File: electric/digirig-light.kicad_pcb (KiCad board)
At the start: 2 copper layers, 12.2 x 37.9 mm, 22 parts, among them J1 USB_A, J2 PJ-320A, Q1 MMBT5551L, U1 CM108B

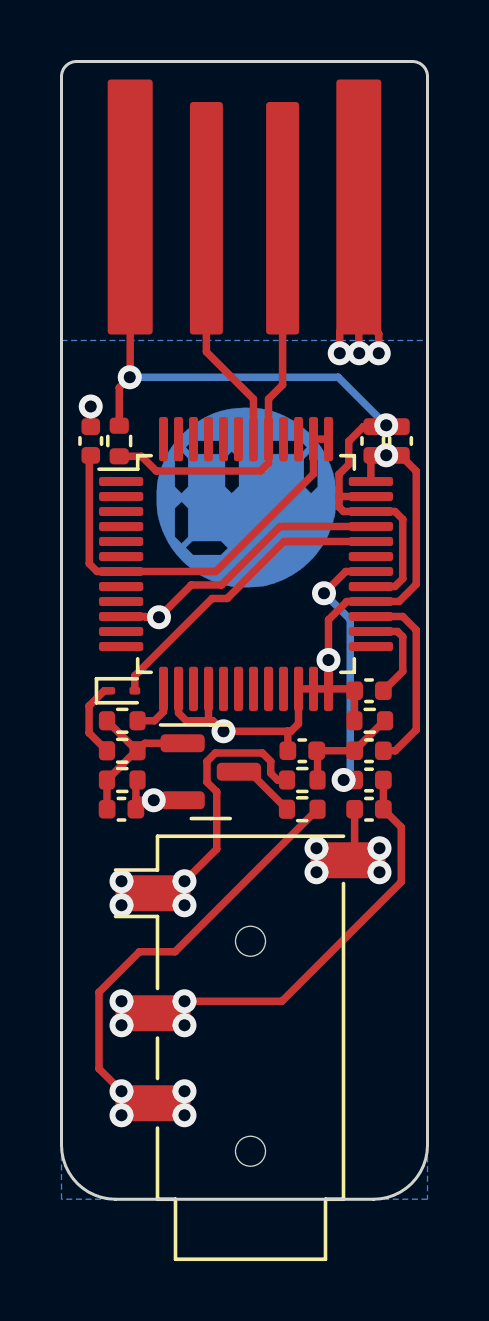
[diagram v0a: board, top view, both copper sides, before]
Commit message: Revision 1.1
- PTT by tone circuit modification
- CM108B output voltage config change from 2.5V to 3.5V
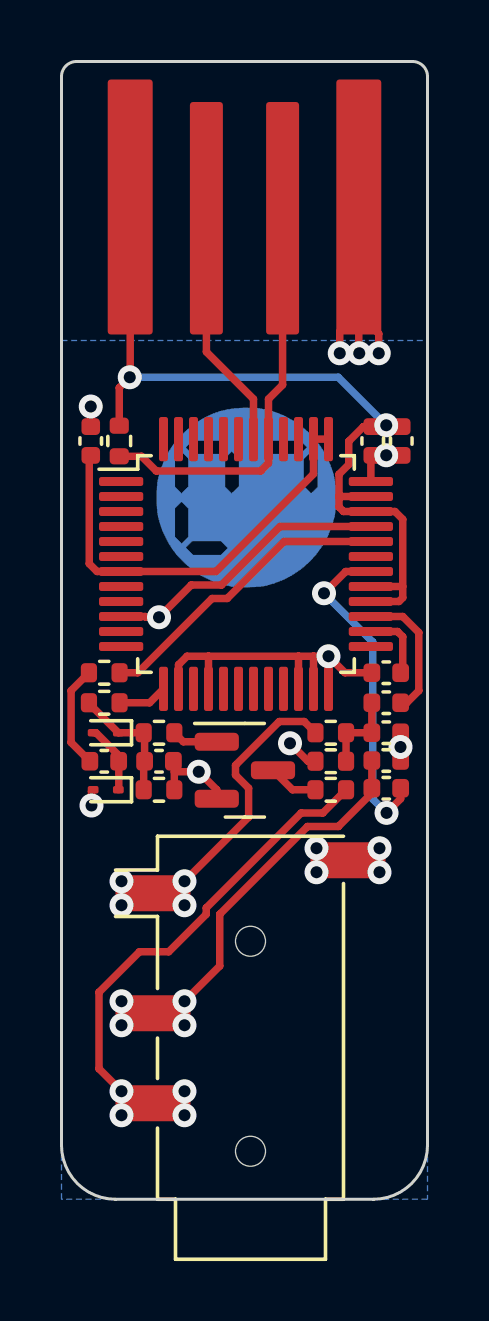
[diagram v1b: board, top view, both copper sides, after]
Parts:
- added C10: 100nF, Capacitor_SMD:C_0402_1005Metric, F.Cu at (139.4, 92.0)
- added D2: GS2005ELD, Diode_SMD:D_SOD-923, F.Cu at (130.0, 91.1)
- added R8: 1K5, Resistor_SMD:R_0402_1005Metric, F.Cu at (137.5, 93.0)
- C4, C6: value 10uF -> 1uF
- C7: value 100n -> 10uF
- C8: value 100nF -> 10uF
- R2: value 22 -> 10K
- R3: value 10K -> 22
- R6: value 10K -> 1K5
- R7: value 1K5 -> 10K
- moved C7 9.51 mm to (139.4, 90.1)
- moved C4 9.13 mm to (130.0, 92.0)
- moved C6 7.03 mm to (131.8, 92.0), turned to 0 degrees
- moved R6 5.03 mm to (131.8, 91.1), turned to 180 degrees
- moved D1 3.35 mm to (130.0, 93.0), turned to 180 degrees
- moved C8 3.07 mm to (139.4, 92.9), turned to 0 degrees
- moved R7 2.72 mm to (137.5, 91.1), turned to 0 degrees
- moved C5 2.66 mm to (139.4, 89.1), turned to 180 degrees
- moved C9 2.61 mm to (139.4, 91.1), turned to 0 degrees
- moved R4 1.87 mm to (137.5, 92.0)
- moved R2 1.71 mm to (130.0, 90.1)
- moved R3 1.71 mm to (130.0, 89.1), turned to 180 degrees
- moved R5 1.27 mm to (131.8, 93.0)
- moved Q1 1.14 mm to (134.7, 92.3)
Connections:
- C4 pad 1: Net-(U1-VREF) -> Net-(D1-K)
- C4 pad 2: GND -> Net-(C4-Pad2)
- C5 pad 1: Net-(C5-Pad1) -> Net-(U1-VREF)
- C5 pad 2: Net-(U1-MICIN) -> GND
- C6 pad 1: /RIG_AFIN -> Net-(D2-K)
- C6 pad 2: Net-(U1-LOL) -> GND
- C7 pad 1: Net-(Q1-B) -> Net-(C7-Pad1)
- C7 pad 2: GND -> Net-(U1-MICIN)
- C8 pad 1: Net-(C5-Pad1) -> /RIG_AFIN
- C8 pad 2: GND -> Net-(U1-LOL)
- C9 pad 1: /RIG_AFIN -> Net-(C7-Pad1)
- D1 pad 2: /ROUT -> GND
- R2 pad 1: Net-(D1-K) -> Net-(D2-K)
- R2 pad 2: Net-(Q1-B) -> /PTT
- R3 pad 1: Net-(Q1-B) -> /ROUT
- R3 pad 2: /PTT -> Net-(C4-Pad2)
- R4 pad 1: Net-(C5-Pad1) -> Net-(C7-Pad1)
- R5 pad 2: Net-(Q1-B) -> Net-(D2-K)
- R6 pad 1: /RIG_AFOUT -> Net-(Q1-B)
- R6 pad 2: Net-(C5-Pad1) -> Net-(D2-K)
- R7 pad 1: /RIG_PTT -> /RIG_AFOUT
- R7 pad 2: Net-(Q1-C) -> Net-(C7-Pad1)
- U1 pad 28: GND -> +5V
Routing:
- net GND: track 52.8 -> 44.7 mm, vias 13 -> 15
- net Net-(D2-K): track 0.00 -> 4.18 mm
- net Net-(Q1-B): track 5.44 -> 1.54 mm
- net Net-(C5-Pad1): track 3.68 -> 0.00 mm
- net Net-(C4-Pad2): track 0.00 -> 3.46 mm
- net Net-(C7-Pad1): track 0.00 -> 2.81 mm
- net Net-(U1-LOL): track 8.90 -> 11.1 mm
- net Net-(U1-MICIN): track 6.41 -> 4.53 mm
- net +5V: track 27.4 -> 29.1 mm
- net /RIG_PTT: track 13.4 -> 14.8 mm
- net /RIG_AFIN: track 12.5 -> 11.2 mm
- net Net-(U1-VREF): track 3.20 -> 2.36 mm
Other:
- board text added: "Rev 1.1 https://digirig.net"
- board text removed: "Rev 1.0 https://digirig.net"
